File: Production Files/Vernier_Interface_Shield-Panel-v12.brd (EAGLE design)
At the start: 166.6 x 156.5 mm, 179 parts, among them U1 74HC4052SO, U2 LMV358SOICT, U3 74HC4052SO, U4 LMV358SOICT, U5 74HC4052SO, U6 LMV358SOICT, U7 74HC4052SO, U8 LMV358SOICT

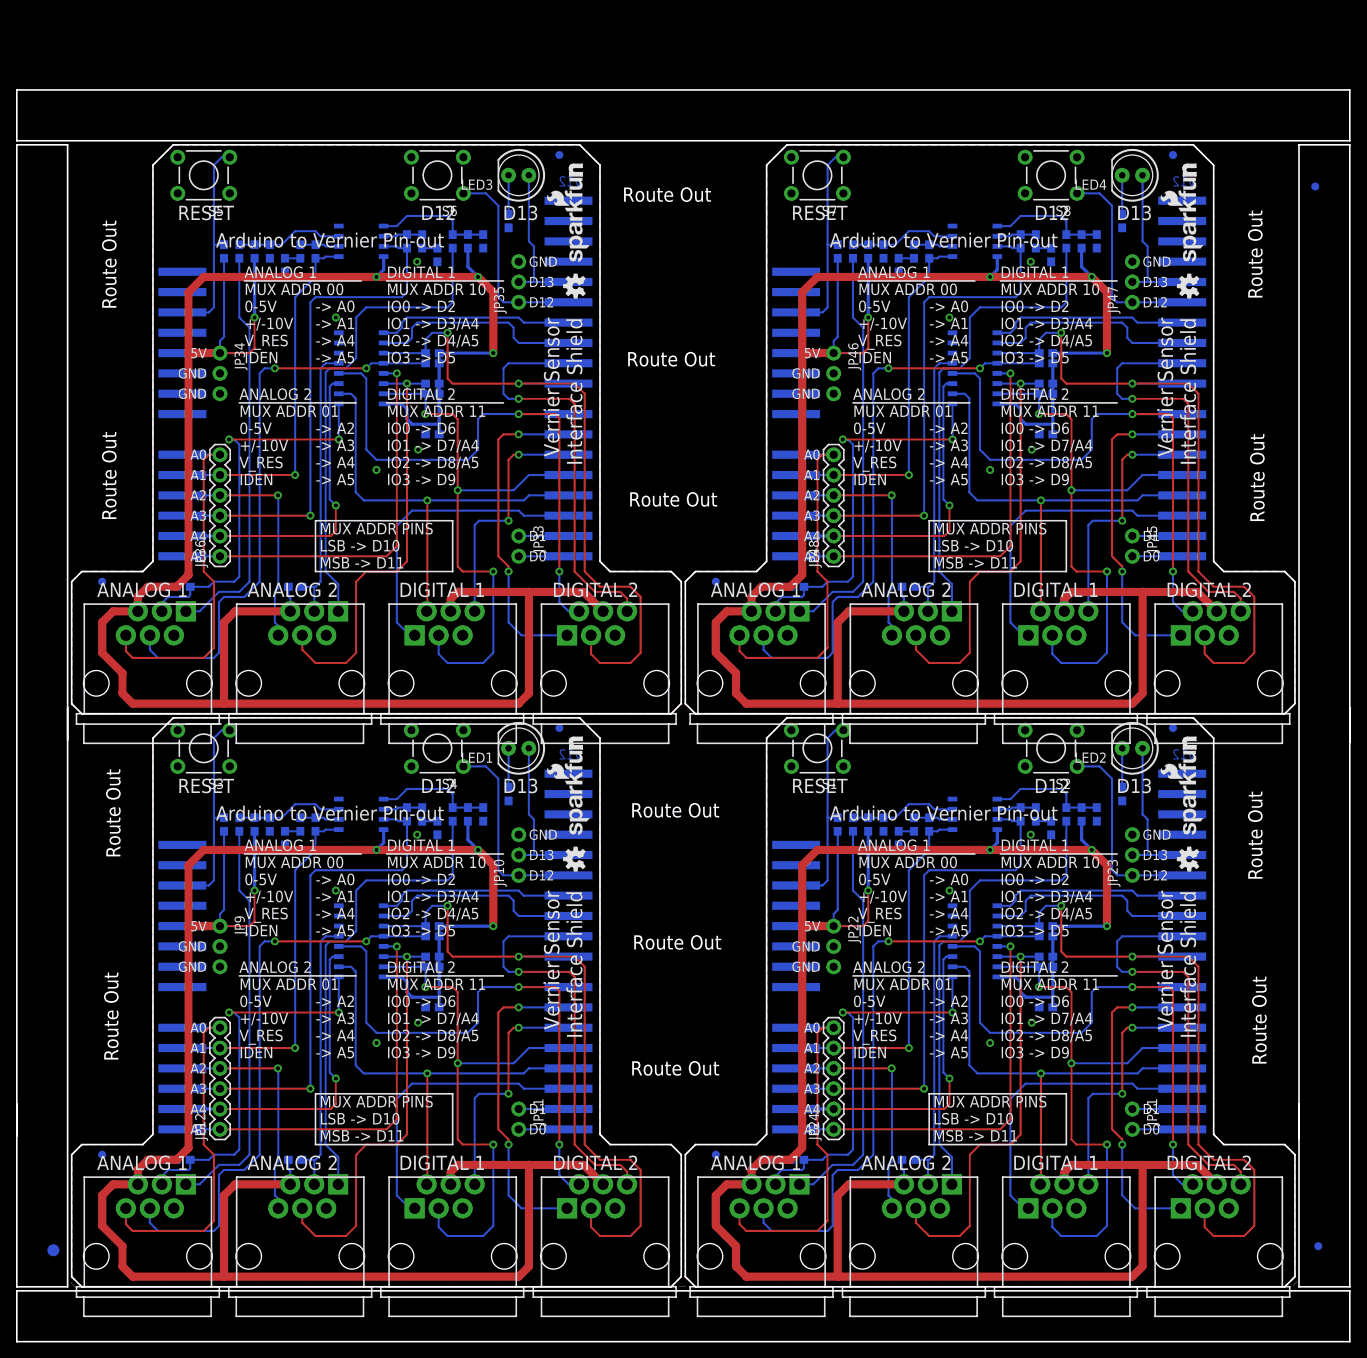
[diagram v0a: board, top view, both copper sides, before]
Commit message: re-created panel v12 with proper spacing
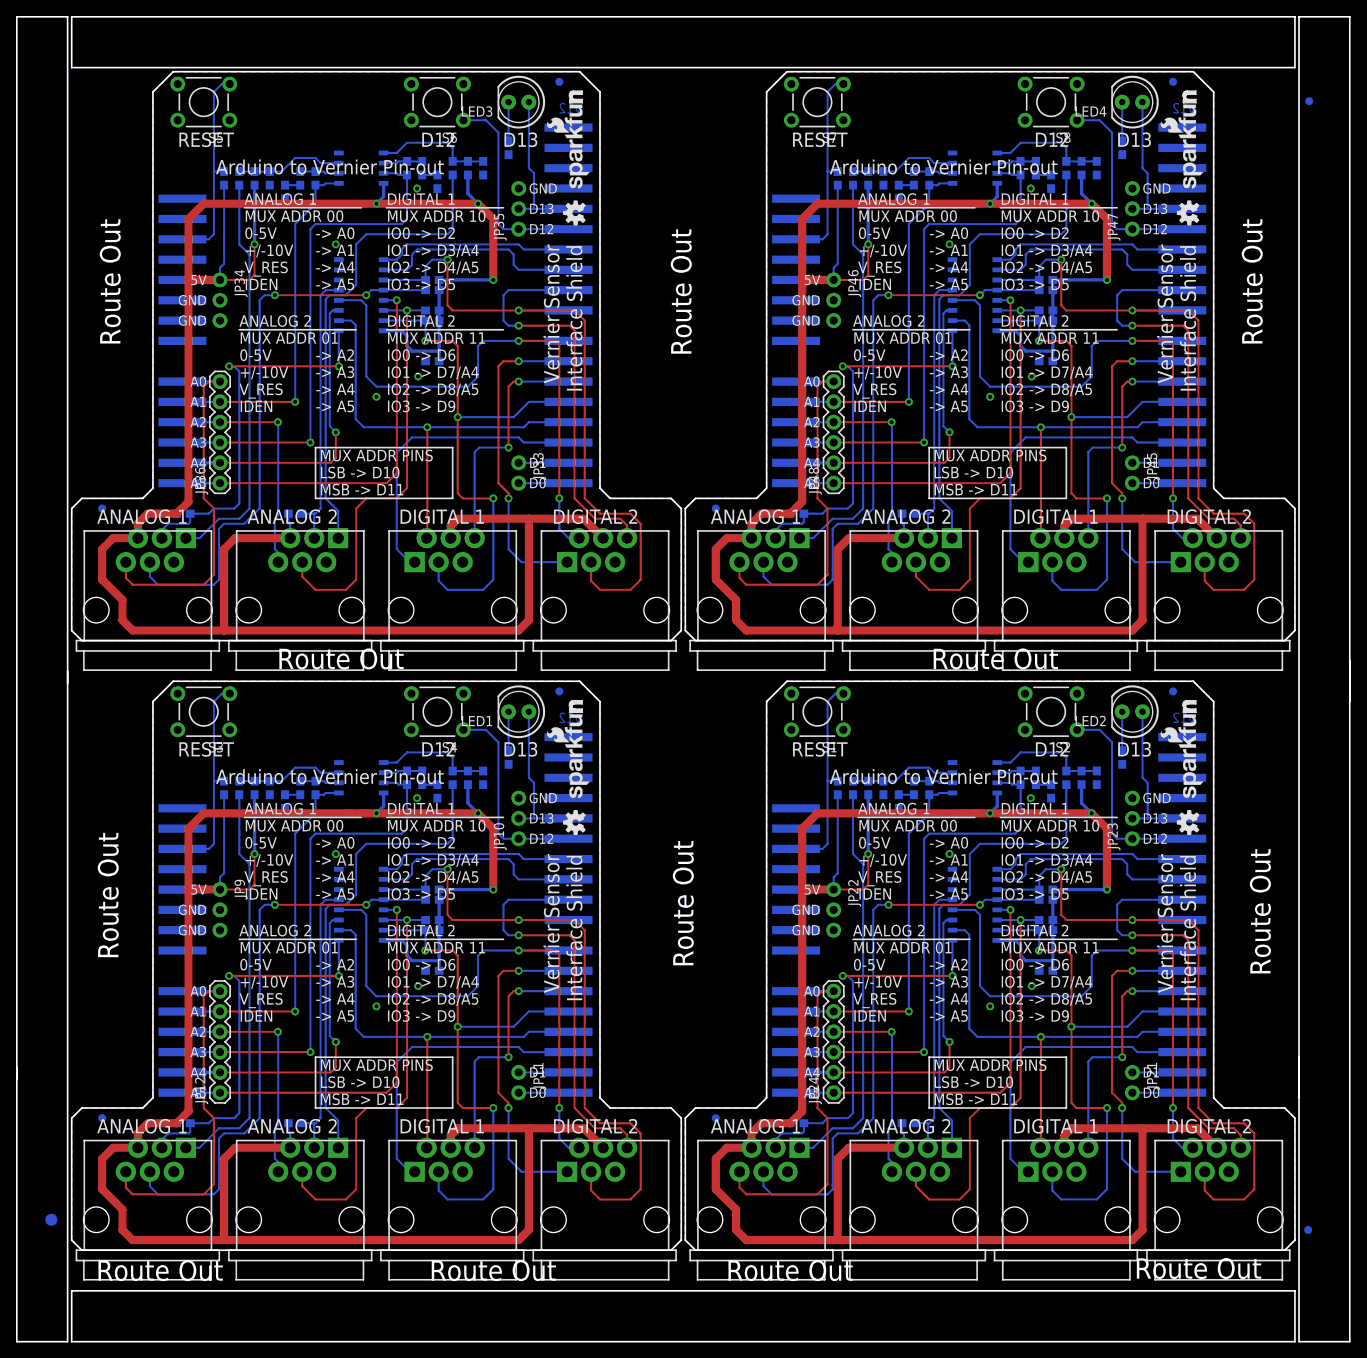
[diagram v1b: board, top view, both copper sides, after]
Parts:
- moved E$6 10.7 mm to (161.5, 155.1), turned to 270 degrees
- moved C5 9.14 mm to (42.4, 142.2)
- moved C6 9.14 mm to (51.9, 122.6)
- moved C7 9.14 mm to (119.1, 142.2)
- moved C8 9.14 mm to (128.7, 122.6)
- moved FID5 9.14 mm to (10.7, 104.1)
- moved FID7 9.14 mm to (87.4, 104.1)
- moved JP25 9.14 mm to (69.0, 128.9)
- moved JP27 9.14 mm to (20.7, 125.1)
- moved JP33 9.14 mm to (62.7, 109.9)
- moved JP34 9.14 mm to (25.4, 132.7)
- moved JP35 9.14 mm to (62.7, 139.1)
- moved JP37 9.14 mm to (145.7, 128.9)
- moved JP39 9.14 mm to (97.4, 125.1)
- moved JP45 9.14 mm to (139.4, 109.9)
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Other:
- board size 166.6 x 156.5 mm -> 166.6 x 165.6 mm
